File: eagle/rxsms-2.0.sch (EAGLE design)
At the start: 156 parts, among them Q1 opt, Q10 BSS123, Q11 BSS123, Q12 BSS123, Q2 BSS123, Q3 BSS123, Q4 BSS123, Q5 BSS123, Q6 BSS123, Q7 BSS123, Q8 BSS123, Q9 BSS123, T10_SODS SWITCH_LED, T1_LO SMS_IP67, T2_SOE SMS_IP67, T3_SOE SWITCH_LED, T4_PWR SMS_IP67, T5_ERRINH SMS_IP67, T6_PWR SWITCH_LED, T7_ERRINH SWITCH_LED, T8_LO SWITCH_LED, T9_SODS SMS_IP67, U1 MAX3232ESE, U2 XMEGA-A4UTQFP, U3 TSR_1-2450, U4 LM1117, U5 NC7WZ17P6X, U6 ADUM3160, U7 TPS73125, U8 NUP2202W1, X1 PN61729-S, X5 RLP2-200-500

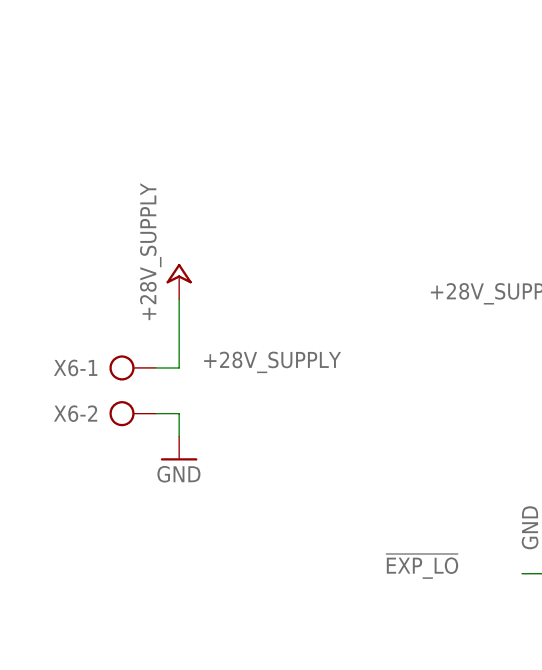
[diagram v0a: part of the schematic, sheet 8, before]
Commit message: added 4mm jacks for supply
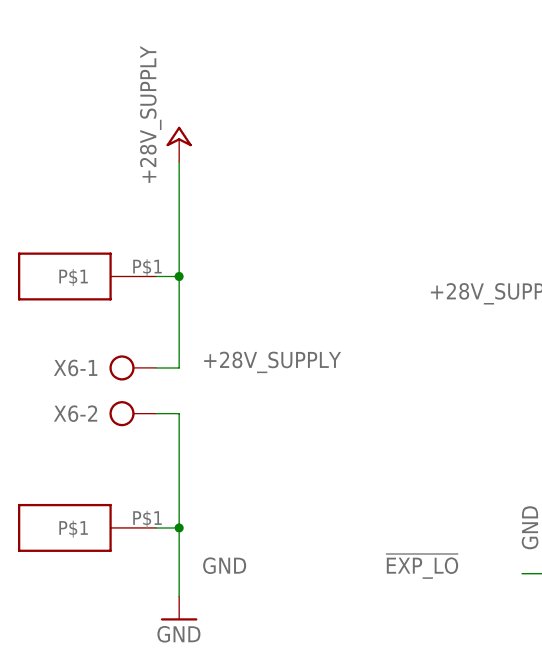
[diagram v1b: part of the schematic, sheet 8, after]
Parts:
- added U$3, U$9: JACK, jack:JACK
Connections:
- net +28V_SUPPLY: now also U$9.P$1
- net GND: now also U$3.P$1
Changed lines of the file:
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@@
 <part name="SJ6" library="jumper" deviceset="SJ" device=""/>
 <part name="P+16" library="supply1" deviceset="+24V" device="" value="+28V_SUPPLY"/>
+<part name="U$3" library="jack" deviceset="JACK" device=""/>
+<part name="U$9" library="jack" deviceset="JACK" device=""/>
 </parts>
 <sheets>
@@
 <instance part="X6" gate="-1" x="60.96" y="119.38"/>
 <instance part="X6" gate="-2" x="60.96" y="114.3"/>
-<instance part="P+15" gate="1" x="68.58" y="129.54"/>
-<instance part="GND40" gate="1" x="68.58" y="109.22"/>
+<instance part="P+15" gate="1" x="68.58" y="144.78"/>
+<instance part="GND40" gate="1" x="68.58" y="91.44"/>
 <instance part="GND38" gate="1" x="109.22" y="101.6" rot="R270"/>
+<instance part="U$3" gate="G$1" x="60.96" y="101.6" rot="R180"/>
+<instance part="U$9" gate="G$1" x="60.96" y="129.54" rot="R180"/>
 </instances>
 <busses>
@@
 <pinref part="P+15" gate="1" pin="+24V"/>
 <wire x1="66.04" y1="119.38" x2="68.58" y2="119.38" width="0.1524" layer="91"/>
-<wire x1="68.58" y1="119.38" x2="68.58" y2="127" width="0.1524" layer="91"/>
+<wire x1="68.58" y1="119.38" x2="68.58" y2="129.54" width="0.1524" layer="91"/>
 <label x="71.12" y="119.38" size="1.778" layer="95"/>
+<pinref part="U$9" gate="G$1" pin="P$1"/>
+<wire x1="68.58" y1="129.54" x2="68.58" y2="142.24" width="0.1524" layer="91"/>
+<wire x1="66.04" y1="129.54" x2="68.58" y2="129.54" width="0.1524" layer="91"/>
+<junction x="68.58" y="129.54"/>
 </segment>
 </net>
@@
 <pinref part="GND40" gate="1" pin="GND"/>
 <wire x1="66.04" y1="114.3" x2="68.58" y2="114.3" width="0.1524" layer="91"/>
-<wire x1="68.58" y1="114.3" x2="68.58" y2="111.76" width="0.1524" layer="91"/>
+<wire x1="68.58" y1="114.3" x2="68.58" y2="101.6" width="0.1524" layer="91"/>
+<pinref part="U$3" gate="G$1" pin="P$1"/>
+<wire x1="68.58" y1="101.6" x2="68.58" y2="93.98" width="0.1524" layer="91"/>
+<wire x1="66.04" y1="101.6" x2="68.58" y2="101.6" width="0.1524" layer="91"/>
+<junction x="68.58" y="101.6"/>
+<label x="71.12" y="96.52" size="1.778" layer="95"/>
 </segment>
 <segment>

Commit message: several ordercodes updated
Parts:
- C34: OC_FARNELL 1759241 -> 2407305
- R12, R13: OC_FARNELL 1894163 -> (none); OC_RS (none) -> 666-2386
- R48: OC_FARNELL 2332111 -> 2333544
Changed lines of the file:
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@@
 </part>
 <part name="R12" library="rcl" deviceset="R-EU_" device="R0805" value="24/1%">
-<attribute name="OC_FARNELL" value="1894163"/>
+<attribute name="OC_RS" value="666-2386"/>
 </part>
 <part name="GND12" library="supply1" deviceset="GND" device=""/>
@@
 </part>
 <part name="R13" library="rcl" deviceset="R-EU_" device="R0805" value="24/1%">
-<attribute name="OC_FARNELL" value="1894163"/>
+<attribute name="OC_RS" value="666-2386"/>
 </part>
 <part name="C19" library="rcl" deviceset="C-EU" device="C0805K" value="1u">
@@
 </part>
 <part name="C34" library="rcl" deviceset="C-EU" device="C0805K" value="4n7">
-<attribute name="OC_FARNELL" value="1759241"/>
+<attribute name="OC_FARNELL" value="2407305"/>
 </part>
 <part name="R48" library="rcl" deviceset="R-EU_" device="R0805" value="1M">
-<attribute name="OC_FARNELL" value="2332111"/>
+<attribute name="OC_FARNELL" value="2333544"/>
 </part>
 <part name="LED7" library="led" deviceset="LED" device="CHIPLED_1206" value="BERNSTEIN">
@@
 </instance>
 <instance part="R12" gate="G$1" x="76.2" y="66.04">
-<attribute name="OC_FARNELL" x="76.2" y="66.04" size="1.778" layer="96" display="off"/>
+<attribute name="OC_RS" x="76.2" y="66.04" size="1.778" layer="96" display="off"/>
 </instance>
 <instance part="GND12" gate="1" x="-7.62" y="48.26"/>
@@
 </instance>
 <instance part="R13" gate="G$1" x="76.2" y="58.42">
-<attribute name="OC_FARNELL" x="76.2" y="58.42" size="1.778" layer="96" display="off"/>
+<attribute name="OC_RS" x="76.2" y="58.42" size="1.778" layer="96" display="off"/>
 </instance>
 <instance part="C19" gate="G$1" x="2.54" y="76.2">

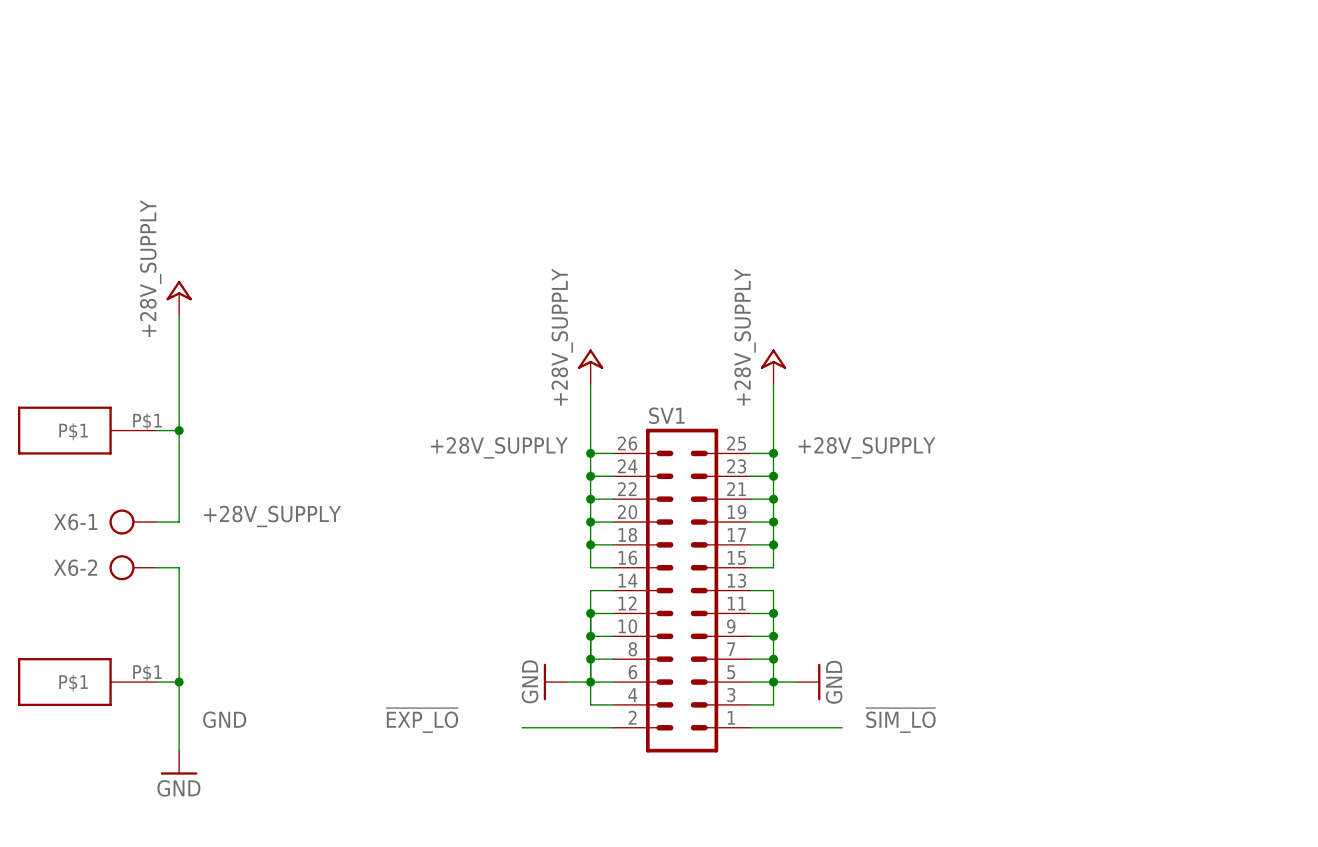
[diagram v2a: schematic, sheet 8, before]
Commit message: add reverse input voltage protection
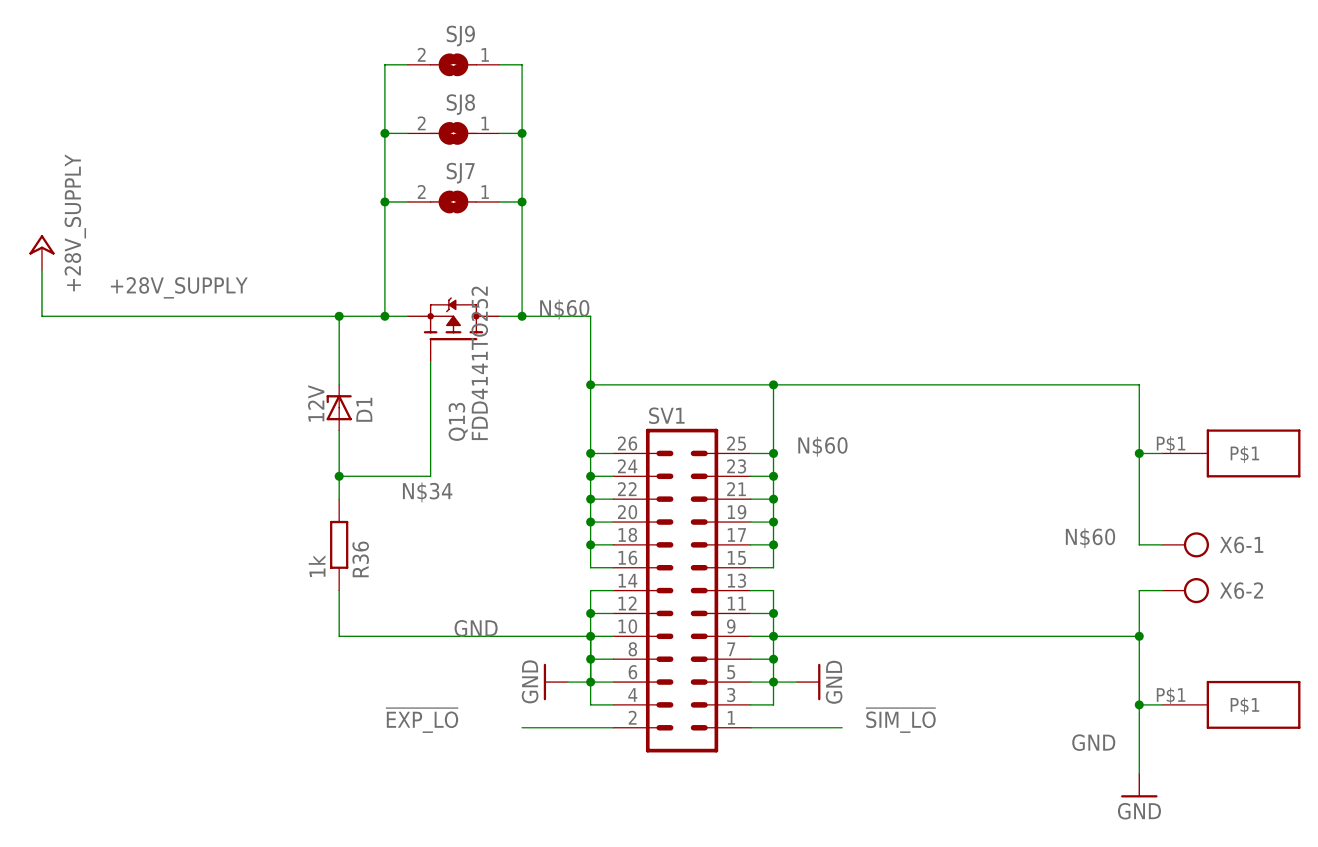
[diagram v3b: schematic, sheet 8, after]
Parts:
- added D1: 12V, diode:ZENER-DIODEDO34-7
- added Q13: FDD4141TO252, transistor-fet:FDD4141TO252
- added R36: 1k, rcl:R-EU_R0805
- added SJ7, SJ8, SJ9: (no value), jumper:SJ
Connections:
- new net N$34: D1.A, Q13.G, R36.2
- new net N$60: Q13.D, SJ7.1, SJ8.1, SJ9.1, SV1.15, SV1.16, SV1.17, SV1.18, SV1.19, SV1.20, SV1.21, SV1.22, SV1.23, SV1.24, SV1.25, SV1.26, U$9.P$1, X6-1.KL
- net +28V_SUPPLY: now also D1.C, Q13.S, SJ7.2, SJ8.2, SJ9.2; no longer SV1.15, SV1.16, SV1.17, SV1.18, SV1.19, SV1.20, SV1.21, SV1.22, SV1.23, SV1.24, SV1.25, SV1.26, U$9.P$1, X6-1.KL
- net GND: now also R36.1
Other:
- moved on the sheet: X6-1, X6-2

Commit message: OC for 1k resistor updated
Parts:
- R16, R17, R18, R19, R20, R43, R44: OC_FARNELL 9237496 -> 2332071
- R46, R47: OC_FARNELL 9237496/2332058 -> 2332071/2332058
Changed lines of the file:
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@@
 </part>
 <part name="R19" library="rcl" deviceset="R-EU_" device="R0805" value="1k">
-<attribute name="OC_FARNELL" value="9237496"/>
+<attribute name="OC_FARNELL" value="2332071"/>
 </part>
 <part name="C28" library="rcl" deviceset="C-EU" device="C0805K" value="100n">
@@
 <part name="GND20" library="supply1" deviceset="GND" device=""/>
 <part name="R20" library="rcl" deviceset="R-EU_" device="R0805" value="1k">
-<attribute name="OC_FARNELL" value="9237496"/>
+<attribute name="OC_FARNELL" value="2332071"/>
 </part>
 <part name="C29" library="rcl" deviceset="C-EU" device="C0805K" value="100n">
@@
 <part name="GND28" library="supply1" deviceset="GND" device=""/>
 <part name="R16" library="rcl" deviceset="R-EU_" device="R0805" value="1k">
-<attribute name="OC_FARNELL" value="9237496"/>
+<attribute name="OC_FARNELL" value="2332071"/>
 </part>
 <part name="C25" library="rcl" deviceset="C-EU" device="C0805K" value="100n">
@@
 </part>
 <part name="R17" library="rcl" deviceset="R-EU_" device="R0805" value="1k">
-<attribute name="OC_FARNELL" value="9237496"/>
+<attribute name="OC_FARNELL" value="2332071"/>
 </part>
 <part name="C26" library="rcl" deviceset="C-EU" device="C0805K" value="100n">
@@
 <part name="GND29" library="supply1" deviceset="GND" device=""/>
 <part name="R18" library="rcl" deviceset="R-EU_" device="R0805" value="1k">
-<attribute name="OC_FARNELL" value="9237496"/>
+<attribute name="OC_FARNELL" value="2332071"/>
 </part>
 <part name="C27" library="rcl" deviceset="C-EU" device="C0805K" value="100n">
@@
 </part>
 <part name="R43" library="rcl" deviceset="R-EU_" device="R0805" value="1k">
-<attribute name="OC_FARNELL" value="9237496"/>
+<attribute name="OC_FARNELL" value="2332071"/>
 </part>
 <part name="T5_ERRINH" library="SMSIp67" deviceset="SMS_IP67" device="">
@@
 </part>
 <part name="R44" library="rcl" deviceset="R-EU_" device="R0805" value="1k">
-<attribute name="OC_FARNELL" value="9237496"/>
+<attribute name="OC_FARNELL" value="2332071"/>
 </part>
 <part name="R46" library="rcl" deviceset="R-EU_" device="R0805" value="1k/100">
-<attribute name="OC_FARNELL" value="9237496/2332058"/>
+<attribute name="OC_FARNELL" value="2332071/2332058"/>
 </part>
 <part name="LED6" library="led" deviceset="LED" device="CHIPLED_1206" value="BERNSTEIN">
@@
 </part>
 <part name="R47" library="rcl" deviceset="R-EU_" device="R0805" value="1k/100">
-<attribute name="OC_FARNELL" value="9237496/2332058"/>
+<attribute name="OC_FARNELL" value="2332071/2332058"/>
 </part>
 <part name="GND32" library="supply1" deviceset="GND" device=""/>

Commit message: OC for 270 ohm resistor updated
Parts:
- R29, R32: OC_FARNELL 2008375 -> 2332064; OC_RS 740-9019 -> (none)
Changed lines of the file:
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@@
 </part>
 <part name="R29" library="rcl" deviceset="R-EU_" device="R0805" value="270">
-<attribute name="OC_FARNELL" value="2008375"/>
-<attribute name="OC_RS" value="740-9019"/>
+<attribute name="OC_FARNELL" value="2332064"/>
 </part>
 <part name="VDD5" library="supply1" deviceset="VDD" device=""/>
@@
 </part>
 <part name="R32" library="rcl" deviceset="R-EU_" device="R0805" value="270">
-<attribute name="OC_FARNELL" value="2008375"/>
-<attribute name="OC_RS" value="740-9019"/>
+<attribute name="OC_FARNELL" value="2332064"/>
 </part>
 <part name="VDD6" library="supply1" deviceset="VDD" device=""/>
@@
 </instance>
 <instance part="R29" gate="G$1" x="101.6" y="119.38" rot="R90">
-<attribute name="OC_RS" x="101.6" y="119.38" size="1.778" layer="96" rot="R90" display="off"/>
 <attribute name="OC_FARNELL" x="101.6" y="119.38" size="1.778" layer="96" rot="R90" display="off"/>
 </instance>
@@
 </instance>
 <instance part="R32" gate="G$1" x="101.6" y="38.1" rot="R90">
-<attribute name="OC_RS" x="101.6" y="38.1" size="1.778" layer="96" rot="R90" display="off"/>
 <attribute name="OC_FARNELL" x="101.6" y="38.1" size="1.778" layer="96" rot="R90" display="off"/>
 </instance>

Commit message: OC for 4u7/50V capacitor updated
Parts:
- C12, C13, C30, C31, C35: OC_FARNELL 2210979 -> 2346932
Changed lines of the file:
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@@
 </part>
 <part name="C12" library="rcl" deviceset="C-EU" device="C0805K" value="4u7/50V">
-<attribute name="OC_FARNELL" value="2210979"/>
+<attribute name="OC_FARNELL" value="2346932"/>
 </part>
 <part name="C13" library="rcl" deviceset="C-EU" device="C0805K" value="4u7/50V">
-<attribute name="OC_FARNELL" value="2210979"/>
+<attribute name="OC_FARNELL" value="2346932"/>
 </part>
 <part name="+3V3" library="supply1" deviceset="+3V3" device=""/>
@@
 <part name="U$10" library="TEN3" deviceset="TEN3-2410N" device=""/>
 <part name="C30" library="rcl" deviceset="C-EU" device="C0805K" value="4u7/50V">
-<attribute name="OC_FARNELL" value="2210979"/>
+<attribute name="OC_FARNELL" value="2346932"/>
 </part>
 <part name="P+4" library="supply1" deviceset="+24V" device="" value="+28V_SUPPLY"/>
 <part name="U$11" library="Coil" deviceset="COIL" device=""/>
 <part name="C31" library="rcl" deviceset="C-EU" device="C0805K" value="4u7/50V">
-<attribute name="OC_FARNELL" value="2210979"/>
+<attribute name="OC_FARNELL" value="2346932"/>
 </part>
 <part name="C35" library="rcl" deviceset="C-EU" device="C0805K" value="4u7/50V">
-<attribute name="OC_FARNELL" value="2210979"/>
+<attribute name="OC_FARNELL" value="2346932"/>
 </part>
 <part name="U$12" library="Coil" deviceset="COIL" device=""/>

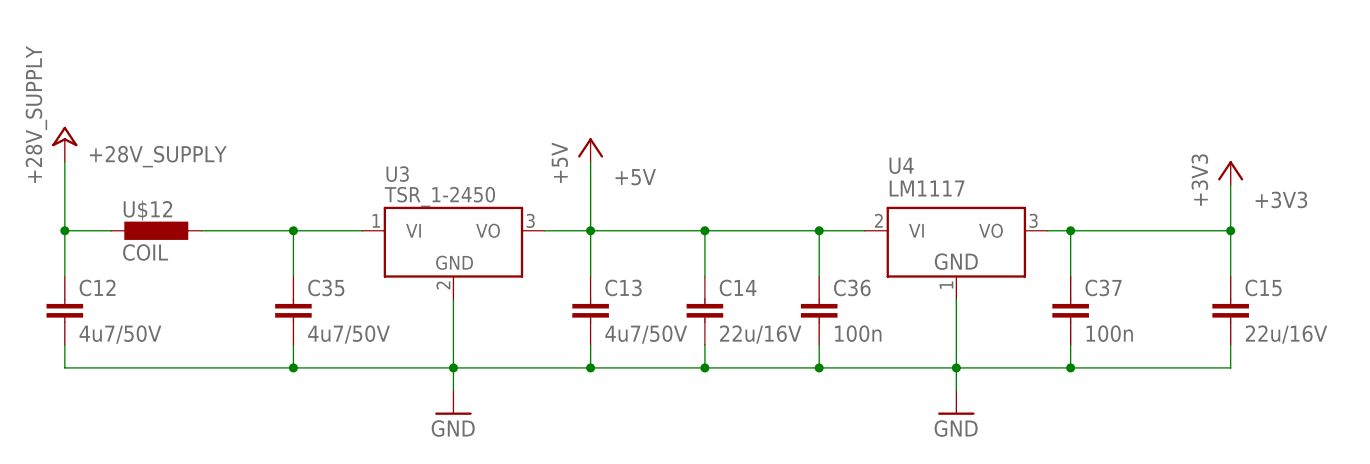
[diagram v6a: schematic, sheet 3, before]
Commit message: OC for 22u capacitor updated, increase vtg rating from 16V to 25V
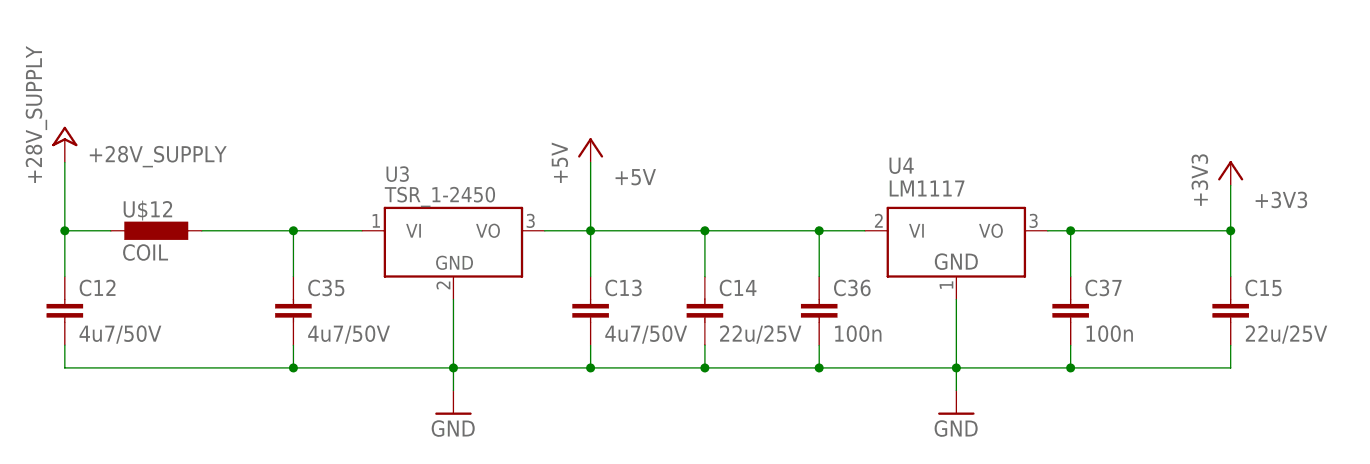
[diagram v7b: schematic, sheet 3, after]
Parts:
- C14, C15: value 22u/16V -> 22u/25V; OC_FARNELL 2346925 -> 1907510
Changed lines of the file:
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@@
 <part name="P+2" library="supply1" deviceset="+24V" device="" value="+28V_SUPPLY"/>
 <part name="P+3" library="supply1" deviceset="+5V" device=""/>
-<part name="C14" library="rcl" deviceset="C-EU" device="C0805K" value="22u/16V">
-<attribute name="OC_FARNELL" value="2346925"/>
+<part name="C14" library="rcl" deviceset="C-EU" device="C0805K" value="22u/25V">
+<attribute name="OC_FARNELL" value="1907510"/>
 </part>
-<part name="C15" library="rcl" deviceset="C-EU" device="C0805K" value="22u/16V">
-<attribute name="OC_FARNELL" value="2346925"/>
+<part name="C15" library="rcl" deviceset="C-EU" device="C0805K" value="22u/25V">
+<attribute name="OC_FARNELL" value="1907510"/>
 </part>
 <part name="GND4" library="supply1" deviceset="GND" device=""/>

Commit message: fix prefix for coil
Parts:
- renumbered U$11 to L1, U$12 to L2
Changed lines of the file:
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@@
 </part>
 <part name="P+4" library="supply1" deviceset="+24V" device="" value="+28V_SUPPLY"/>
-<part name="U$11" library="Coil" deviceset="COIL" device=""/>
+<part name="L1" library="Coil" deviceset="COIL" device=""/>
 <part name="C31" library="rcl" deviceset="C-EU" device="C0805K" value="4u7/50V">
 <attribute name="OC_FARNELL" value="2346932"/>
@@
 <attribute name="OC_FARNELL" value="2346932"/>
 </part>
-<part name="U$12" library="Coil" deviceset="COIL" device=""/>
+<part name="L2" library="Coil" deviceset="COIL" device=""/>
 <part name="C36" library="rcl" deviceset="C-EU" device="C0805K" value="100n">
 <attribute name="OC_FARNELL" value="1759265"/>
@@
 </instance>
 <instance part="P+4" gate="1" x="152.4" y="165.1"/>
-<instance part="U$11" gate="G$1" x="162.56" y="160.02"/>
+<instance part="L1" gate="G$1" x="162.56" y="160.02"/>
 <instance part="C31" gate="G$1" x="170.18" y="154.94">
 <attribute name="OC_FARNELL" x="170.18" y="154.94" size="1.778" layer="96" display="off"/>
@@
 <wire x1="185.42" y1="157.48" x2="177.8" y2="157.48" width="0.1524" layer="91"/>
 <wire x1="177.8" y1="157.48" x2="177.8" y2="160.02" width="0.1524" layer="91"/>
-<pinref part="U$11" gate="G$1" pin="1"/>
+<pinref part="L1" gate="G$1" pin="1"/>
 <wire x1="167.64" y1="160.02" x2="170.18" y2="160.02" width="0.1524" layer="91"/>
 <junction x="177.8" y="160.02"/>
@@
 <wire x1="152.4" y1="162.56" x2="152.4" y2="160.02" width="0.1524" layer="91"/>
 <pinref part="C30" gate="G$1" pin="1"/>
-<pinref part="U$11" gate="G$1" pin="2"/>
+<pinref part="L1" gate="G$1" pin="2"/>
 <wire x1="152.4" y1="160.02" x2="152.4" y2="157.48" width="0.1524" layer="91"/>
 <wire x1="157.48" y1="160.02" x2="152.4" y2="160.02" width="0.1524" layer="91"/>
@@
 <attribute name="OC_FARNELL" x="60.96" y="116.84" size="1.778" layer="96" display="off"/>
 </instance>
-<instance part="U$12" gate="G$1" x="45.72" y="124.46"/>
+<instance part="L2" gate="G$1" x="45.72" y="124.46"/>
 <instance part="C36" gate="G$1" x="119.38" y="116.84">
 <attribute name="OC_FARNELL" x="119.38" y="116.84" size="1.778" layer="96" display="off"/>
@@
 <pinref part="C12" gate="G$1" pin="1"/>
 <label x="38.1" y="132.08" size="1.778" layer="95"/>
-<pinref part="U$12" gate="G$1" pin="2"/>
+<pinref part="L2" gate="G$1" pin="2"/>
 <wire x1="35.56" y1="124.46" x2="35.56" y2="119.38" width="0.1524" layer="91"/>
 <wire x1="40.64" y1="124.46" x2="35.56" y2="124.46" width="0.1524" layer="91"/>
@@
 <net name="VI" class="0">
 <segment>
-<pinref part="U$12" gate="G$1" pin="1"/>
+<pinref part="L2" gate="G$1" pin="1"/>
 <pinref part="U3" gate="G$1" pin="VI"/>
 <wire x1="50.8" y1="124.46" x2="60.96" y2="124.46" width="0.1524" layer="91"/>
